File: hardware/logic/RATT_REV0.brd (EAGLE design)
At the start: 127 x 76.2 mm, 132 parts, among them IC1 TLP292-4, IC13 MCP73831, IC16 PCA9539PW, IC2 CPC1002N, IC3 CPC1002N, IC4 CPC1002N, IC5 CPC1002N, J1 4P-2.0, J2 4P-2.0, J3 F-1X06-SIP-100-40, J4 4P-2.0, J6 4P-2.0, J7 PHOENIX1803484, J8 PHOENIX1803484, Q1 2.5A/30V, Q2 MBT3904DW1T1, Q3 2.5A/30V, Q5 2N7002, Q6 2.5A/30V, U1 RPI-ZERO, U5 AP2112K-3.3V

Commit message: Just need to do the dumb power path
I forget what I did, but it wasn't the power path yet
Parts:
- removed C2: 10uF, SparkFun-Capacitors:0805@1
- removed C21: 0.1uF, MakeItLabs:0603-CAP
- removed D1: Yellow, SparkFun-LED:LED-0603
- removed D4: BAT20J, SparkFun-DiscreteSemi:SOD-323
- removed F1: 500mA, SparkFun-PowerIC:PTC-1206
- removed J3: F-1X06-SIP-100-40, con-headers-jp:SIP-100-06-40
- removed SJ2: JUMPER-PAD-2-NC_BY_TRACE, SparkFun-Passives:PAD-JUMPER-2-NC_BY_TRACE_YES_SILK
- added J5: F-1X04-SIP-100-40, con-headers-jp:SIP-100-04-40
- added LED4, LED5, LED6: RED, SparkFun-LED:LED-0603
- added R56, R57: 1K, SparkFun-Resistors:0603
- added R58: 1k, SparkFun-Resistors:0603
- added R59: 10k, SparkFun-Resistors:0603
- IC13: value MCP73831 -> MCP73832
- R24: value 10k -> 1k
- moved R24 181.4 mm to (-54.6, -71.9)
- moved U5 113.8 mm to (-3.81, 90.9), turned to 270 degrees
- moved C22 21.4 mm to (0.25, 90.8), turned to 270 degrees
- moved C1 7.78 mm to (54.4, 66.5)
- moved FB4 6.11 mm to (48.5, 68.1)
- moved C25 4.83 mm to (54.4, 68.0)
- moved R20 2.54 mm to (58.2, 66.8)
- moved R37 2.29 mm to (59.7, 66.8)
- moved FB3 1.02 mm to (48.5, 66.3)
- renumbered X2 to J100
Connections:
- removed net 3.3REG_EN: D4.A
- removed net VUSB-RAW: F1.1
- removed net V_USB: F1.2, FB3.2
- new net N$53: Q2.5, R58.1
- net +3V3: now also R59.2
- net +5V: now also FB3.2, R56.1, R58.2
- net 3.3V: now also R21.1; no longer SJ2.2
- net 5V_RFID_TX: now also J5.3; no longer J3.6
- net CHARGE_STATUS: now also LED6.C, U1.32; no longer D1.C
- net GND: now also J5.1, LED4.C, LED5.C, Q2.4; no longer C2.2, C21.2, J3.1
- net N$12: now also LED5.A, R57.2; no longer R21.1, SJ2.1
- net N$17: now also LED6.A; no longer D1.A
- net N$18: no longer D4.C
- net N$50: now also LED4.A, R56.2; no longer C2.1, C21.1, FB4.1, J3.3
- net N$51: now also FB4.1, J5.2; no longer J3.2
- net PWR_LOSS: now also Q2.3, R59.1
- net RFID_RX: now also J5.4, U1.8; no longer J3.5, U1.10
- net RFID_TX: now also U1.10; no longer U1.8
- net VIN: now also R57.1
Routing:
- net RFID_RX: track 70.4 -> 65.5 mm
- net RFID_TX: track 67.2 -> 70.8 mm

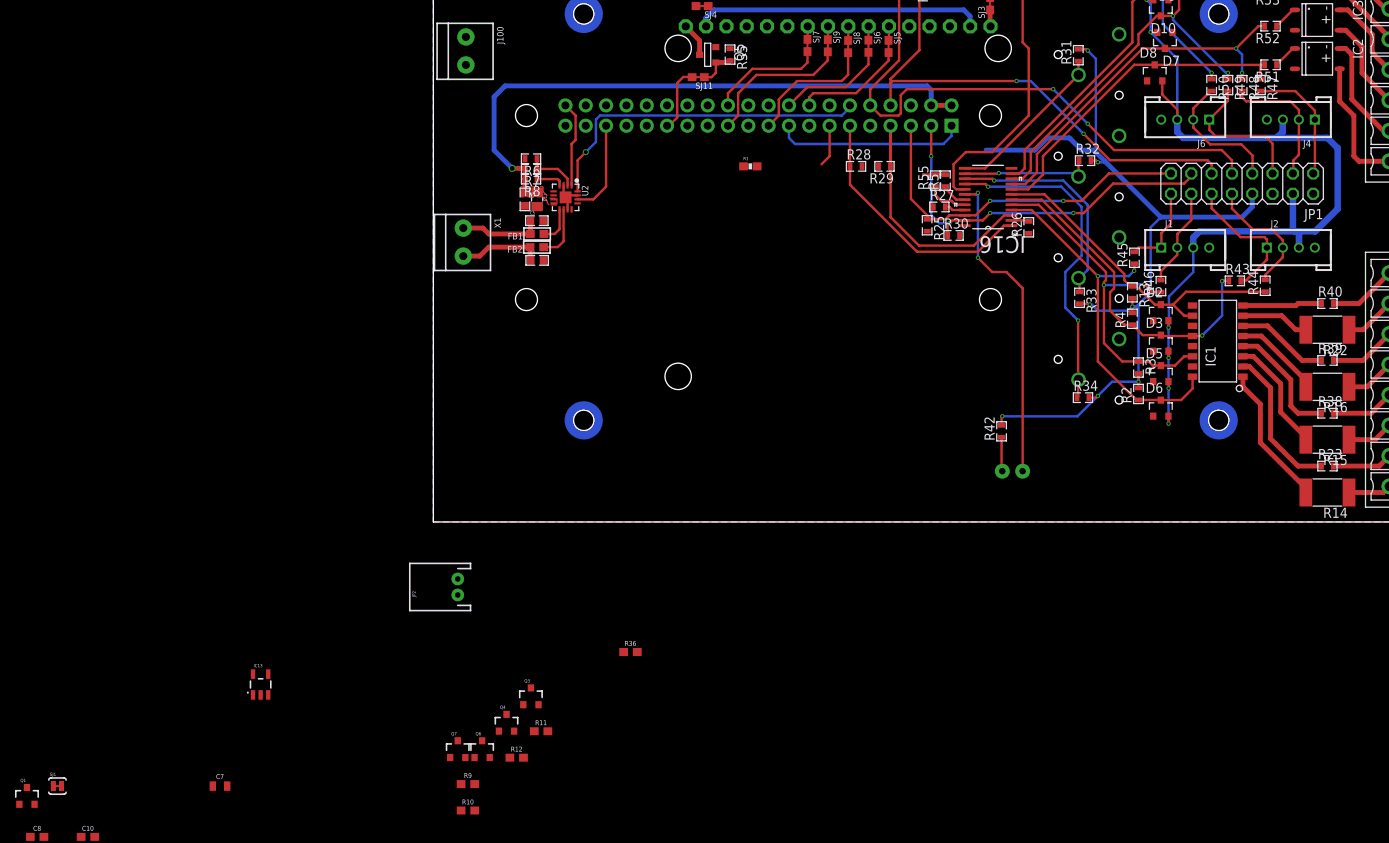
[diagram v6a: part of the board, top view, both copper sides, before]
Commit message: Renamed Power Supply Nets
+5VIN = Input from Dc brick
+5VB = 5V or Battery backed supply
+3.3V = +3.3V supply created from +5VB by either Pi or reg circuit
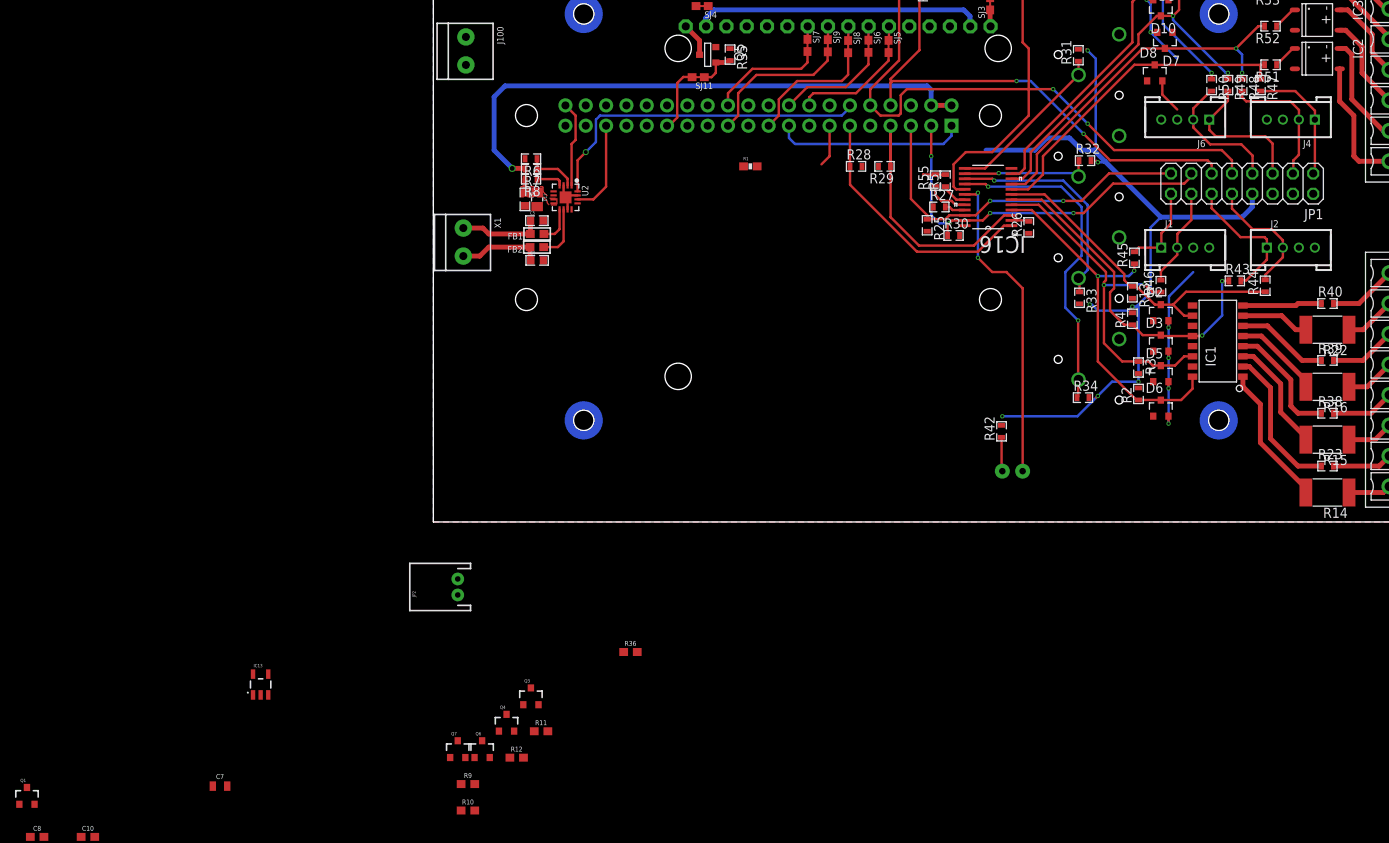
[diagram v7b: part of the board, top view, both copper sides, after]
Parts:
- removed SJ1: JUMPER-PAD-2-NC_BY_TRACE, SparkFun-Passives:PAD-JUMPER-2-NC_BY_TRACE_YES_SILK
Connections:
- removed net +3V3: C18.1, C20.1, C22.1, C23.1, FB4.2, IC16.24, JP1.8, R1.2, R13.2, R2.2, R25.2, R28.2, R29.2, R3.2, R30.2, R31.2, R32.2, R33.2, R34.2, R4.2, R41.2, R42.2, R5.2, R55.2, R59.2, SJ4.2
- removed net +5V: C19.1, D10.2, D2.2, D3.2, D5.2, D6.2, D7.2, D8.2, D9.2, FB3.2, IC13.4, J1.3, J100.1, J2.3, J4.3, J6.3, JP1.4, Q1.1, Q6.3, R17.2, R18.1, R56.1, R58.2, R9.2
- removed net 3.3V: C10.1, R21.1, R36.1, U5.5
- removed net N$16: R19.2, SJ1.1
- removed net VIN: C17.1, C7.1, C9.1, Q1.2, Q6.2, R10.1, R24.2, R57.1, R7.2, R8.2, U1.2, U1.4, U2.7, U2.8, U5.1
- new net +3.3V: C10.1, C18.1, C20.1, C22.1, C23.1, FB4.2, IC16.24, JP1.8, R1.2, R13.2, R2.2, R21.1, R25.2, R28.2, R29.2, R3.2, R30.2, R31.2, R32.2, R33.2, R34.2, R36.1, R4.2, R41.2, R42.2, R5.2, R55.2, R59.2, SJ4.2, U5.5
- new net +5VB: C17.1, C7.1, C9.1, D10.2, D2.2, D3.2, D5.2, D6.2, D7.2, D8.2, D9.2, FB3.2, Q1.2, Q6.2, R10.1, R24.2, R57.1, R7.2, R8.2, U1.2, U1.4, U2.7, U2.8, U5.1
- new net +5VIN: C19.1, IC13.4, J1.3, J100.1, J2.3, J4.3, J6.3, JP1.4, Q1.1, Q6.3, R17.2, R18.1, R56.1, R58.2, R9.2
- net N$14: now also R19.2; no longer SJ1.2
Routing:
- net +5VB: track 0.00 -> 116.6 mm, vias 0 -> 8
- net +5V: track 115.8 -> 0.00 mm, vias 7 -> 0
- net +3V3: track 113.5 -> 0.00 mm, vias 7 -> 0
- net +3.3V: track 0.00 -> 105.2 mm, vias 0 -> 7
- net VIN: track 74.4 -> 0.00 mm, vias 1 -> 0

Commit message: Schematic Done! (ref des and attributes may change)
Initial pass on schematic done.  Ref Des and attributes will change before it is finished though
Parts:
- removed Q1, Q3, Q6: 2.5A/30V, SparkFun-DiscreteSemi:SOT23-3
- removed Q2: MBT3904DW1T1, esp32-thing-temp:SC70-6
- removed Q4, Q7: (no value), DURRIDGE-TRANSISTORS:SOT23-3
- removed R10, R17, R59: 10k, SparkFun-Resistors:0603
- removed R58, R9: 1k, SparkFun-Resistors:0603
- added C2, C3: 0.1uF, SparkFun-Capacitors:0603-CAP@1
- added IC200: TPS2115AIPWRQ1, Texas Instruments_By_element14_Batch_1:SOP65P640X120-8N
- added R60: 1k, SparkFun-Resistors:0603
- added R61: 10k, SparkFun-Resistors:0603
- IC300: value (none) -> MAx98357
- R12: value 1k -> 10k
- moved R11 156.1 mm to (-85.3, -147.1)
- moved R12 154.2 mm to (-85.3, -150.4)
- renumbered U2 to IC300, X1 to J200
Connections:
- removed net !SHUTDOWN: R12.1, U1.13
- removed net N$10: Q1.3, Q3.3
- removed net N$35: Q7.1, R9.1
- removed net N$38: Q4.1, R12.2
- removed net N$53: Q2.5, R58.1
- removed net N$9: Q6.1, Q7.3, R10.2
- removed net PWR_LOSS: Q2.3, R59.1, U1.37
- new net !PWR_LOSS: IC200.1, R61.1, U1.37
- new net SHUTDOWN: IC200.3, R12.2, U1.13
- net +3.3V: now also R61.2; no longer R59.2
- net +5VB: now also IC200.2, IC200.7, R11.2; no longer Q1.2, Q6.2, R10.1
- net +5VIN: now also C3.1, IC200.6; no longer Q1.1, Q6.3, R17.2, R58.2, R9.2
- net GND: now also C2.2, C3.2, IC200.5, R11.1, R12.1, R60.1; no longer Q2.4, Q4.2, Q7.2, R17.1
- net N$37: now also IC200.4, R60.2; no longer Q3.1, Q4.3, R11.1
- net V_BATT: now also C2.1, IC200.8; no longer Q3.2, R11.2
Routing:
- net SHUTDOWN: track 0.00 -> 5.25 mm
- net !SHUTDOWN: track 5.25 -> 0.00 mm
